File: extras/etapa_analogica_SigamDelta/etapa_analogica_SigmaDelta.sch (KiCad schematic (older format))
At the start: 18 parts, among them P1 CONN_01X01, P2 CONN_01X01, P3 CONN_01X01, P4 CONN_01X01, P5 CONN_01X02

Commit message: Mojo Cape edited
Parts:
- removed P1, P2, P3, P4: CONN_01X01, Pin_Headers:Pin_Header_Straight_1x01, symbol CONN_01X01
- removed P5: CONN_01X02, Pin_Headers:Pin_Header_Straight_1x02, symbol CONN_01X02
- added P1, P3: CONN_02X10, symbol CONN_02X10
- added P2: CONN_01X03, symbol CONN_01X03
- added P4: BNC, symbol BNC
- added R5: 5k6, Resistors_SMD:R_0805_HandSoldering, symbol R
- RV2: value 1k -> 10k
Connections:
- net labels added: 3,3v, 3.3v, 5v, N21, N23, N26, N29, N32, N34, N40, N50, P22, P24, P27, P30, P33, P35, P41, P51, Rx, Tx
- net labels removed: Vcc, Vsignal
- wire segments 37 -> 78
- no-connect marks 0 -> 27
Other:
- moved on the sheet: C3, C4, C6, R4, RV1, RV2

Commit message: .
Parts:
- removed R5: 5k6, Resistors_SMD:R_0805_HandSoldering, symbol R
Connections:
- net GND: no longer RV2.2
- net at D1.2 (K), R1.1: now also RV1.1
- net at RV1.2: now also RV1.3, RV2.1; no longer R4.2
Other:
- moved on the sheet: RV1, RV2
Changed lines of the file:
@@
 L POT RV1
 U 1 1 56154BFA
-P 5200 1500
-F 0 "RV1" H 5200 1400 50  0000 C CNN
-F 1 "100" H 5200 1500 50  0000 C CNN
-F 2 "Potentiometers:Potentiometer_Bourns_3296W_3-8Zoll_Inline_ScrewUp" H 5200 1500 60  0001 C CNN
-F 3 "" H 5200 1500 60  0000 C CNN
-	1    5200 1500
-	0    1    1    0
+P 4850 1250
+F 0 "RV1" H 4850 1150 50  0000 C CNN
+F 1 "100" H 4850 1250 50  0000 C CNN
+F 2 "Potentiometers:Potentiometer_Bourns_3296W_3-8Zoll_Inline_ScrewUp" H 4850 1250 60  0001 C CNN
+F 3 "" H 4850 1250 60  0000 C CNN
+	1    4850 1250
+	1    0    0    -1
 $EndComp
 $Comp
@@
 L POT RV2
 U 1 1 5617E04B
-P 5200 2125
-F 0 "RV2" H 5200 2025 50  0000 C CNN
-F 1 "10k" H 5200 2125 50  0000 C CNN
-F 2 "Potentiometers:Potentiometer_Bourns_3296W_3-8Zoll_Inline_ScrewUp" H 5200 2125 60  0001 C CNN
-F 3 "" H 5200 2125 60  0000 C CNN
-	1    5200 2125
+P 5175 1500
+F 0 "RV2" H 5175 1400 50  0000 C CNN
+F 1 "10k" H 5175 1500 50  0000 C CNN
+F 2 "Potentiometers:Potentiometer_Bourns_3296W_3-8Zoll_Inline_ScrewUp" H 5175 1500 60  0001 C CNN
+F 3 "" H 5175 1500 60  0000 C CNN
+	1    5175 1500
 	0    1    1    0
 $EndComp
@@
 Wire Wire Line
 	6475 1500 6475 1750
-Wire Wire Line
-	4500 1250 4500 1625
-Wire Wire Line
-	5200 2525 5200 2375
 Connection ~ 3800 1250
 Wire Wire Line
 	3800 1250 3800 1675
 Connection ~ 3550 1250
-Connection ~ 5200 2525
 Connection ~ 4500 2525
 Connection ~ 3800 2525
@@
 Wire Wire Line
 	5750 1500 6675 1500
-Connection ~ 4500 1250
 Wire Wire Line
 	3250 1250 4000 1250
@@
 $EndComp
 Wire Wire Line
-	5350 2125 5450 2125
-Wire Wire Line
-	5450 2125 5450 2425
-Wire Wire Line
-	5450 2425 5200 2425
-Connection ~ 5200 2425
-Wire Wire Line
 	5350 1500 5450 1500
-Wire Wire Line
-	5200 1750 5200 1875
-$Comp
-L R R5
-U 1 1 561C5510
-P 4800 1250
-F 0 "R5" V 4880 1250 50  0000 C CNN
-F 1 "5k6" V 4800 1250 50  0000 C CNN
-F 2 "Resistors_SMD:R_0805_HandSoldering" V 4730 1250 30  0001 C CNN
-F 3 "" H 4800 1250 30  0000 C CNN
-	1    4800 1250
-	0    1    1    0
-$EndComp
-Wire Wire Line
-	4300 1250 4650 1250
-Wire Wire Line
-	4950 1250 5200 1250
 Wire Wire Line
 	9300 3450 9475 3450
@@
 	4700 2475 4700 2525
 Connection ~ 4700 2525
+Wire Wire Line
+	5100 1250 5175 1250
+Wire Wire Line
+	5175 1750 5175 2525
+Connection ~ 5175 2525
+Wire Wire Line
+	4300 1250 4600 1250
+Wire Wire Line
+	4500 1625 4500 1250
+Connection ~ 4500 1250
+Wire Wire Line
+	4850 1100 5125 1100
+Wire Wire Line
+	5125 1100 5125 1250
+Connection ~ 5125 1250
 $EndSCHEMATC

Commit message: Starting the layout
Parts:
- D1: footprint LEDs:LED-5MM -> Housings_TO-92:TO-92_Rugged_Reverse
- P1, P3: footprint (none) -> Pin_Headers:Pin_Header_Straight_2x10
- P2: footprint (none) -> Pin_Headers:Pin_Header_Straight_1x03
- P4: footprint (none) -> Sockets_BNC:BNC_Socket_TYCO-AMP_LargePads
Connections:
- net 3.3v: no longer P1.3 (P3)
- net Rx: now also P1.12 (P12), P2.2 (P2); no longer P1.8 (P8), P2.1 (P1)
- net Tx: now also P1.14 (P14), P2.1 (P1); no longer P1.10 (P10), P2.2 (P2)
- net at RV2.2: now also R4.2
- net 5v: no longer names the net of P1.1 (P1)
- net 5v: no longer P3.1 (P1)
- no-connect marks 27 -> 31
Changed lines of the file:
@@
 F 0 "D1" V 4600 1825 50  0000 C CNN
 F 1 "LM336" V 4400 1825 50  0000 C CNN
-F 2 "LEDs:LED-5MM" V 4500 1825 60  0001 C CNN
+F 2 "Housings_TO-92:TO-92_Rugged_Reverse" V 4500 1825 60  0001 C CNN
 F 3 "" V 4500 1825 60  0000 C CNN
 	1    4900 1825
@@
 F 0 "P3" H 9050 4050 50  0000 C CNN
 F 1 "CONN_02X10" V 9050 3500 50  0000 C CNN
-F 2 "" H 9050 2300 60  0000 C CNN
+F 2 "Pin_Headers:Pin_Header_Straight_2x10" H 9050 2300 60  0001 C CNN
 F 3 "" H 9050 2300 60  0000 C CNN
 	1    9050 3500
@@
 $EndComp
 Wire Wire Line
-	5350 1500 5450 1500
+	5325 1500 5450 1500
 Wire Wire Line
 	9300 3450 9475 3450
@@
 Text Label 9475 3950 0    60   ~ 0
 P22
-Text Label 8625 3050 2    60   ~ 0
-5v
 Text Label 8625 3150 2    60   ~ 0
 3.3v
@@
 F 0 "P1" H 7000 4150 50  0000 C CNN
 F 1 "CONN_02X10" V 7000 3600 50  0000 C CNN
-F 2 "" H 7000 2400 60  0000 C CNN
+F 2 "Pin_Headers:Pin_Header_Straight_2x10" H 7000 2400 60  0001 C CNN
 F 3 "" H 7000 2400 60  0000 C CNN
 	1    7000 3600
@@
 Text Label 7425 3250 0    60   ~ 0
 GND
-Text Label 6575 3150 2    60   ~ 0
-5v
-Text Label 6575 3250 2    60   ~ 0
-3.3v
 NoConn ~ 7425 3350
 NoConn ~ 6575 3350
@@
 NoConn ~ 7425 3950
 NoConn ~ 7425 3850
-Text Label 7425 3450 0    60   ~ 0
+Text Label 7425 3650 0    60   ~ 0
 Rx
-Text Label 7425 3550 0    60   ~ 0
+Text Label 7425 3750 0    60   ~ 0
 Tx
-NoConn ~ 7425 3750
-NoConn ~ 7425 3650
 $Comp
 L CONN_01X03 P2
@@
 F 0 "P2" H 8900 2500 50  0000 C CNN
 F 1 "CONN_01X03" V 9000 2300 50  0000 C CNN
-F 2 "" H 8900 2300 60  0000 C CNN
+F 2 "Pin_Headers:Pin_Header_Straight_1x03" H 8900 2300 60  0001 C CNN
 F 3 "" H 8900 2300 60  0000 C CNN
 	1    8900 2300
@@
 Wire Wire Line
 	8700 2400 8375 2400
+Text Label 8375 2300 2    60   ~ 0
+Rx
 Text Label 8375 2200 2    60   ~ 0
-Rx
-Text Label 8375 2300 2    60   ~ 0
 Tx
 Text Label 8375 2400 2    60   ~ 0
@@
 F 0 "P4" H 3135 3720 50  0000 C CNN
 F 1 "BNC" V 3235 3540 50  0000 C CNN
-F 2 "" H 3125 3600 60  0000 C CNN
+F 2 "Sockets_BNC:BNC_Socket_TYCO-AMP_LargePads" H 3125 3600 60  0001 C CNN
 F 3 "" H 3125 3600 60  0000 C CNN
 	1    3125 3600
@@
 	5125 1100 5125 1250
 Connection ~ 5125 1250
+NoConn ~ 4650 1825
+NoConn ~ 6575 3250
+NoConn ~ 6575 3150
+NoConn ~ 8625 3050
+NoConn ~ 7425 3550
+NoConn ~ 7425 3450
 $EndSCHEMATC

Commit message: Revert "Starting the layout"
This reverts commit 84db6e4c9a3b0a09193008fcb0844fcb533dafef.
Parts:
- D1: footprint Housings_TO-92:TO-92_Rugged_Reverse -> LEDs:LED-5MM
- P1, P3: footprint Pin_Headers:Pin_Header_Straight_2x10 -> (none)
- P2: footprint Pin_Headers:Pin_Header_Straight_1x03 -> (none)
- P4: footprint Sockets_BNC:BNC_Socket_TYCO-AMP_LargePads -> (none)
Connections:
- net 3.3v: now also P1.3 (P3)
- net Rx: now also P1.8 (P8), P2.1 (P1); no longer P1.12 (P12), P2.2 (P2)
- net Tx: now also P1.10 (P10), P2.2 (P2); no longer P1.14 (P14), P2.1 (P1)
- net at RV2.2: no longer R4.2
- net 5v: now reaches P1.1 (P1)
- net 5v: now also P3.1 (P1)
- no-connect marks 31 -> 27
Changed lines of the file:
@@
 F 0 "D1" V 4600 1825 50  0000 C CNN
 F 1 "LM336" V 4400 1825 50  0000 C CNN
-F 2 "Housings_TO-92:TO-92_Rugged_Reverse" V 4500 1825 60  0001 C CNN
+F 2 "LEDs:LED-5MM" V 4500 1825 60  0001 C CNN
 F 3 "" V 4500 1825 60  0000 C CNN
 	1    4900 1825
@@
 F 0 "P3" H 9050 4050 50  0000 C CNN
 F 1 "CONN_02X10" V 9050 3500 50  0000 C CNN
-F 2 "Pin_Headers:Pin_Header_Straight_2x10" H 9050 2300 60  0001 C CNN
+F 2 "" H 9050 2300 60  0000 C CNN
 F 3 "" H 9050 2300 60  0000 C CNN
 	1    9050 3500
@@
 $EndComp
 Wire Wire Line
-	5325 1500 5450 1500
+	5350 1500 5450 1500
 Wire Wire Line
 	9300 3450 9475 3450
@@
 Text Label 9475 3950 0    60   ~ 0
 P22
+Text Label 8625 3050 2    60   ~ 0
+5v
 Text Label 8625 3150 2    60   ~ 0
 3.3v
@@
 F 0 "P1" H 7000 4150 50  0000 C CNN
 F 1 "CONN_02X10" V 7000 3600 50  0000 C CNN
-F 2 "Pin_Headers:Pin_Header_Straight_2x10" H 7000 2400 60  0001 C CNN
+F 2 "" H 7000 2400 60  0000 C CNN
 F 3 "" H 7000 2400 60  0000 C CNN
 	1    7000 3600
@@
 Text Label 7425 3250 0    60   ~ 0
 GND
+Text Label 6575 3150 2    60   ~ 0
+5v
+Text Label 6575 3250 2    60   ~ 0
+3.3v
 NoConn ~ 7425 3350
 NoConn ~ 6575 3350
@@
 NoConn ~ 7425 3950
 NoConn ~ 7425 3850
-Text Label 7425 3650 0    60   ~ 0
+Text Label 7425 3450 0    60   ~ 0
 Rx
-Text Label 7425 3750 0    60   ~ 0
+Text Label 7425 3550 0    60   ~ 0
 Tx
+NoConn ~ 7425 3750
+NoConn ~ 7425 3650
 $Comp
 L CONN_01X03 P2
@@
 F 0 "P2" H 8900 2500 50  0000 C CNN
 F 1 "CONN_01X03" V 9000 2300 50  0000 C CNN
-F 2 "Pin_Headers:Pin_Header_Straight_1x03" H 8900 2300 60  0001 C CNN
+F 2 "" H 8900 2300 60  0000 C CNN
 F 3 "" H 8900 2300 60  0000 C CNN
 	1    8900 2300
@@
 Wire Wire Line
 	8700 2400 8375 2400
+Text Label 8375 2200 2    60   ~ 0
+Rx
 Text Label 8375 2300 2    60   ~ 0
-Rx
-Text Label 8375 2200 2    60   ~ 0
 Tx
 Text Label 8375 2400 2    60   ~ 0
@@
 F 0 "P4" H 3135 3720 50  0000 C CNN
 F 1 "BNC" V 3235 3540 50  0000 C CNN
-F 2 "Sockets_BNC:BNC_Socket_TYCO-AMP_LargePads" H 3125 3600 60  0001 C CNN
+F 2 "" H 3125 3600 60  0000 C CNN
 F 3 "" H 3125 3600 60  0000 C CNN
 	1    3125 3600
@@
 	5125 1100 5125 1250
 Connection ~ 5125 1250
-NoConn ~ 4650 1825
-NoConn ~ 6575 3250
-NoConn ~ 6575 3150
-NoConn ~ 8625 3050
-NoConn ~ 7425 3550
-NoConn ~ 7425 3450
 $EndSCHEMATC

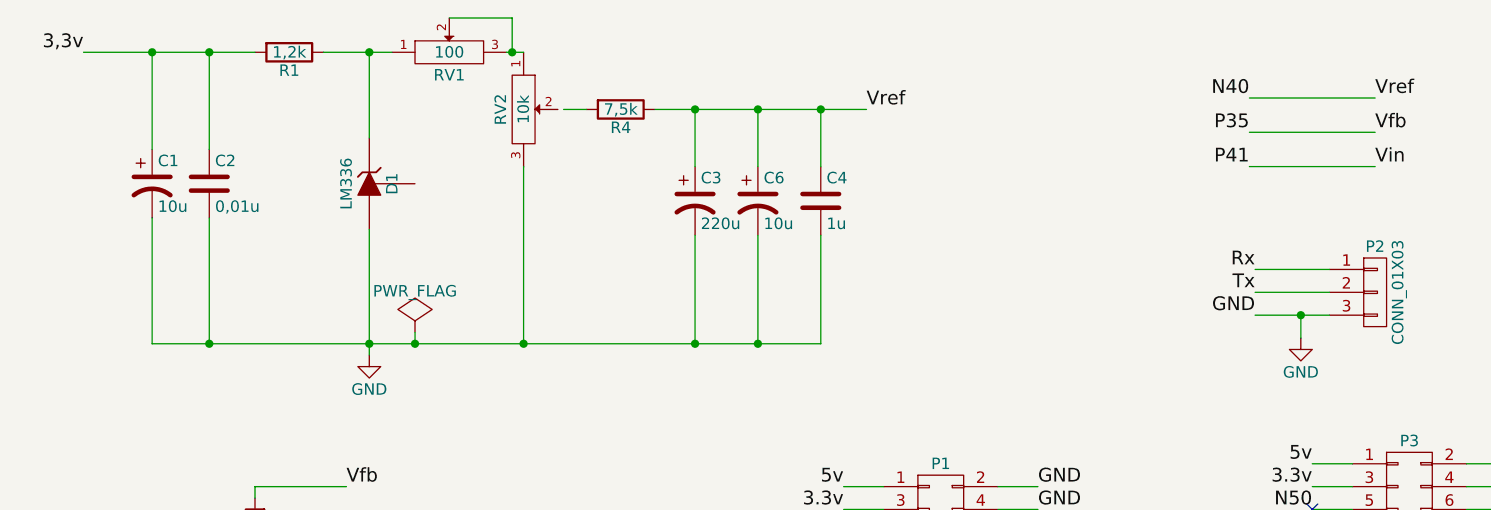
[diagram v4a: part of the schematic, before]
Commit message: Se agregan Rs en Vref. Se modifica R1
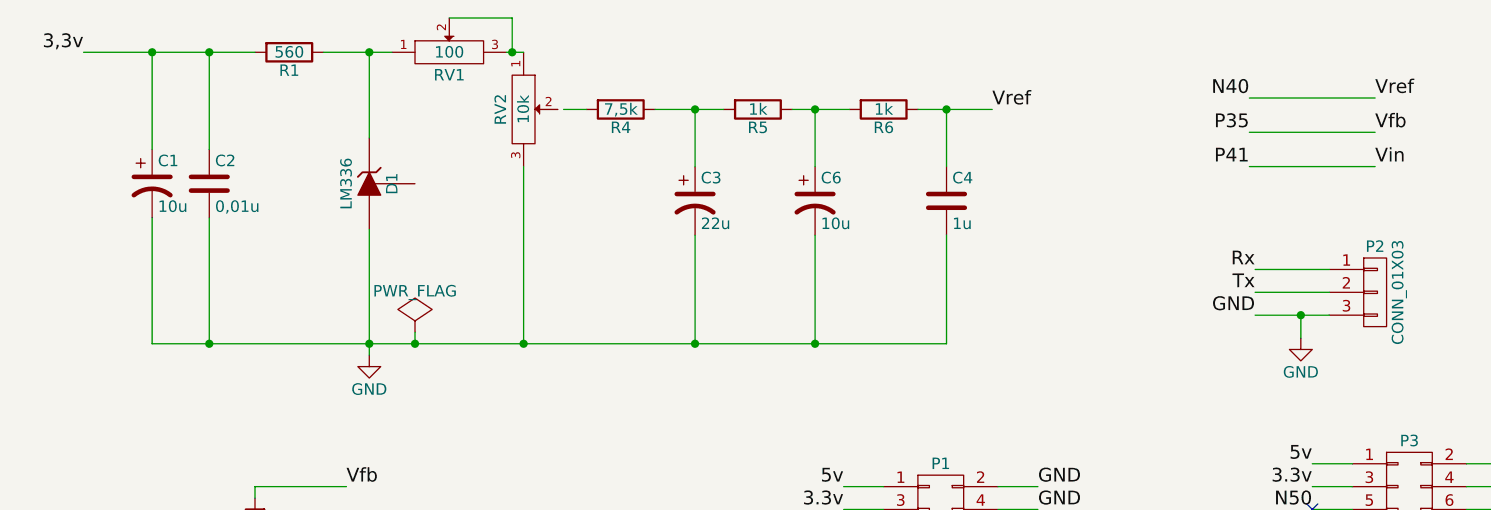
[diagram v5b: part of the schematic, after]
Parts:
- added R5, R6: 1k, Resistors_SMD:R_0805_HandSoldering, symbol R
- C3: value 220u -> 22u
- R1: value 1,2k -> 560
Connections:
- net N40: now also R6.1; no longer C3.1, C6.1, R4.1
- new net: C3.1, R4.1, R5.2
- new net: C6.1, R5.1, R6.2
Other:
- moved on the sheet: C4, C6
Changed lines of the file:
@@
 P 4150 1250
 F 0 "R1" V 4230 1250 50  0000 C CNN
-F 1 "1,2k" V 4150 1250 50  0000 C CNN
+F 1 "560" V 4150 1250 50  0000 C CNN
 F 2 "Resistors_SMD:R_0805_HandSoldering" V 4080 1250 30  0001 C CNN
 F 3 "" H 4150 1250 30  0000 C CNN
@@
 L C C4
 U 1 1 56154D38
-P 6475 1900
-F 0 "C4" H 6500 2000 50  0000 L CNN
-F 1 "1u" H 6500 1800 50  0000 L CNN
-F 2 "Capacitors_SMD:C_0805" H 6513 1750 30  0001 C CNN
-F 3 "" H 6475 1900 60  0000 C CNN
-	1    6475 1900
+P 7025 1900
+F 0 "C4" H 7050 2000 50  0000 L CNN
+F 1 "1u" H 7050 1800 50  0000 L CNN
+F 2 "Capacitors_SMD:C_0805" H 7063 1750 30  0001 C CNN
+F 3 "" H 7025 1900 60  0000 C CNN
+	1    7025 1900
 	1    0    0    -1
 $EndComp
@@
 $EndComp
 $Comp
-L GND #PWR01
+L GND #PWR3
 U 1 1 5615637B
 P 4500 2575
-F 0 "#PWR01" H 4500 2325 50  0001 C CNN
+F 0 "#PWR3" H 4500 2325 50  0001 C CNN
 F 1 "GND" H 4500 2425 50  0000 C CNN
 F 2 "" H 4500 2575 60  0000 C CNN
@@
 $EndComp
 $Comp
-L GND #PWR02
+L GND #PWR2
 U 1 1 561564F5
 P 4000 4050
-F 0 "#PWR02" H 4000 3800 50  0001 C CNN
+F 0 "#PWR2" H 4000 3800 50  0001 C CNN
 F 1 "GND" H 4000 3900 50  0000 C CNN
 F 2 "" H 4000 4050 60  0000 C CNN
@@
 P 5925 1900
 F 0 "C3" H 5950 2000 50  0000 L CNN
-F 1 "220u" H 5950 1800 50  0000 L CNN
+F 1 "22u" H 5950 1800 50  0000 L CNN
 F 2 "Capacitors_SMD:c_elec_4x5.7" H 5925 1900 60  0001 C CNN
 F 3 "" H 5925 1900 60  0000 C CNN
@@
 L CP1 C6
 U 1 1 5617FBFD
-P 6200 1900
-F 0 "C6" H 6225 2000 50  0000 L CNN
-F 1 "10u" H 6225 1800 50  0000 L CNN
-F 2 "Capacitors_Tantalum_SMD:TantalC_SizeA_EIA-3216_HandSoldering" H 6200 1900 60  0001 C CNN
-F 3 "" H 6200 1900 60  0000 C CNN
-	1    6200 1900
+P 6450 1900
+F 0 "C6" H 6475 2000 50  0000 L CNN
+F 1 "10u" H 6475 1800 50  0000 L CNN
+F 2 "Capacitors_Tantalum_SMD:TantalC_SizeA_EIA-3216_HandSoldering" H 6450 1900 60  0001 C CNN
+F 3 "" H 6450 1900 60  0000 C CNN
+	1    6450 1900
 	1    0    0    -1
 $EndComp
@@
 Wire Wire Line
 	5925 2525 5925 2050
-Connection ~ 6200 2525
-Wire Wire Line
-	6200 2525 6200 2050
-Connection ~ 6200 1500
-Wire Wire Line
-	6200 1500 6200 1750
+Connection ~ 6450 2525
+Wire Wire Line
+	6450 2525 6450 2050
+Connection ~ 6450 1500
+Wire Wire Line
+	6450 1500 6450 1750
 Connection ~ 5925 1500
 Wire Wire Line
-	6475 1500 6475 1750
+	7025 1500 7025 1750
 Connection ~ 3800 1250
 Wire Wire Line
@@
 Connection ~ 3800 2525
 Wire Wire Line
-	3550 2525 6475 2525
+	3550 2525 7025 2525
 Wire Wire Line
 	4000 4050 4000 4000
 Wire Wire Line
-	6475 2525 6475 2050
+	7025 2525 7025 2050
 Wire Wire Line
 	4500 2025 4500 2575
@@
 Wire Wire Line
 	3275 3600 3550 3600
-Connection ~ 6475 1500
-Wire Wire Line
-	5750 1500 6675 1500
+Connection ~ 7025 1500
+Wire Wire Line
+	5750 1500 6050 1500
+Wire Wire Line
+	6350 1500 6600 1500
+Wire Wire Line
+	6900 1500 7225 1500
 Wire Wire Line
 	3250 1250 4000 1250
@@
 Text Label 3250 1250 2    60   ~ 0
 3,3v
-Text Label 6675 1500 0    60   ~ 0
+Text Label 7225 1500 0    60   ~ 0
 Vref
 Wire Wire Line
@@
 	8700 2300 8375 2300
 Wire Wire Line
-	8700 2400 8375 2400
+	8375 2400 8700 2400
 Text Label 8375 2200 2    60   ~ 0
 Rx
@@
 $EndComp
 $Comp
-L GND #PWR03
+L GND #PWR1
 U 1 1 561CA0F5
 P 3125 3925
-F 0 "#PWR03" H 3125 3675 50  0001 C CNN
+F 0 "#PWR1" H 3125 3675 50  0001 C CNN
 F 1 "GND" H 3125 3775 50  0000 C CNN
 F 2 "" H 3125 3925 60  0000 C CNN
@@
 	3125 3925 3125 3800
 $Comp
-L GND #PWR04
+L GND #PWR4
 U 1 1 561CA2C4
 P 8575 2500
-F 0 "#PWR04" H 8575 2250 50  0001 C CNN
+F 0 "#PWR4" H 8575 2250 50  0001 C CNN
 F 1 "GND" H 8575 2350 50  0000 C CNN
 F 2 "" H 8575 2500 60  0000 C CNN
@@
 Connection ~ 8575 2400
 $Comp
-L PWR_FLAG #FLG05
+L PWR_FLAG #FLG1
 U 1 1 561CAC5A
 P 4700 2475
-F 0 "#FLG05" H 4700 2570 50  0001 C CNN
+F 0 "#FLG1" H 4700 2570 50  0001 C CNN
 F 1 "PWR_FLAG" H 4700 2655 50  0000 C CNN
 F 2 "" H 4700 2475 60  0000 C CNN
@@
 	5125 1100 5125 1250
 Connection ~ 5125 1250
+$Comp
+L R R5
+U 1 1 561C553D
+P 6200 1500
+F 0 "R5" V 6280 1500 50  0000 C CNN
+F 1 "1k" V 6200 1500 50  0000 C CNN
+F 2 "Resistors_SMD:R_0805_HandSoldering" V 6130 1500 30  0001 C CNN
+F 3 "" H 6200 1500 30  0000 C CNN
+	1    6200 1500
+	0    1    1    0
+$EndComp
+$Comp
+L R R6
+U 1 1 561C588E
+P 6750 1500
+F 0 "R6" V 6830 1500 50  0000 C CNN
+F 1 "1k" V 6750 1500 50  0000 C CNN
+F 2 "Resistors_SMD:R_0805_HandSoldering" V 6680 1500 30  0001 C CNN
+F 3 "" H 6750 1500 30  0000 C CNN
+	1    6750 1500
+	0    1    1    0
+$EndComp
 $EndSCHEMATC
